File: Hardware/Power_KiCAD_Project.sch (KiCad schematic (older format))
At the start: 7 parts, among them J1 Barrel_Jack_MountingPin, J2 XT60 Cell 5, J3 XT60 Cell 4, J4 XT60 Cell 3, J5 XT60 Cell 2, J6 XT60 Cell 1, J7 XT60 To External Switch

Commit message: Routed GNDREF side of board
Correcting keepout silkscreen added 3mm to top and bottom, much appreciated!
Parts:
- J1: symbol Connector:Barrel_Jack_MountingPin -> RDT_Custom_Symbols:Barrel_Jack_MountingPin
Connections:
- net GND: now also J1.2, J1.3 (MountPin)
- removed net GNDREF: J1.2, J1.MP (MountPin)
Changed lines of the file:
@@
 Text Notes 9600 750  2    100  ~ 0
 Temperature Sensors
-$Sheet
-S 8250 2000 800  800
-U 61B35621
-F0 "MCP9808_2" 50
-F1 "COMPONENT_SHEETS/TEMPSENSOR_MCP9808.sch" 50
-F2 "SDA" I L 8250 2550 50
-F3 "SCL" I L 8250 2700 50
-F4 "A0" I R 9050 2150 50
-F5 "A1" I R 9050 2300 50
-F6 "A2" I R 9050 2450 50
-F7 "ALERT" I L 8250 2150 50
-$EndSheet
 Entry Wire Line
 	6750 1900 6650 1800
@@
 	3100 3500 3100 3150
 $Comp
-L power:GNDREF #PWR02
-U 1 1 61C61481
-P 1200 7300
-F 0 "#PWR02" H 1200 7050 50  0001 C CNN
-F 1 "GNDREF" H 1205 7127 50  0000 C CNN
-F 2 "" H 1200 7300 50  0001 C CNN
-F 3 "" H 1200 7300 50  0001 C CNN
-	1    1200 7300
-	1    0    0    -1
-$EndComp
-$Comp
 L Power_KiCAD_Project-rescue:XT60-M-XT60-M-Power_KiCAD_Project-rescue J6
 U 1 1 61C66D12
@@
 $EndComp
 $Comp
-L Connector:Barrel_Jack_MountingPin J1
+L RDT_Custom_Symbols:Barrel_Jack_MountingPin J1
 U 1 1 61C18157
 P 1300 2600
@@
 Wire Wire Line
 	1200 7300 1200 7050
-$Comp
-L power:GNDREF #PWR01
-U 1 1 61DF71F4
-P 950 2650
-F 0 "#PWR01" H 950 2400 50  0001 C CNN
-F 1 "GNDREF" H 955 2477 50  0000 C CNN
-F 2 "" H 950 2650 50  0001 C CNN
-F 3 "" H 950 2650 50  0001 C CNN
-	1    950  2650
-	1    0    0    -1
-$EndComp
 Entry Wire Line
 	3000 5900 3100 5800
@@
 NoConn ~ 5050 1700
 NoConn ~ 5050 1800
+$Comp
+L power:GND #PWR0101
+U 1 1 61FD97B5
+P 1200 7300
+AR Path="/61FD97B5" Ref="#PWR0101"  Part="1"
+AR Path="/61A48488/61FD97B5" Ref="#PWR?"  Part="1"
+F 0 "#PWR0101" H 1200 7050 50  0001 C CNN
+F 1 "GND" H 1205 7127 50  0000 C CNN
+F 2 "" H 1200 7300 50  0001 C CNN
+F 3 "" H 1200 7300 50  0001 C CNN
+	1    1200 7300
+	1    0    0    -1
+$EndComp
+$Sheet
+S 8250 2000 800  800
+U 61B35621
+F0 "MCP9808_2" 50
+F1 "COMPONENT_SHEETS/TEMPSENSOR_MCP9808.sch" 50
+F2 "SDA" I L 8250 2550 50
+F3 "SCL" I L 8250 2700 50
+F4 "A0" I R 9050 2150 50
+F5 "A1" I R 9050 2300 50
+F6 "A2" I R 9050 2450 50
+F7 "ALERT" I L 8250 2150 50
+$EndSheet
+$Comp
+L power:GND #PWR0102
+U 1 1 6208BBED
+P 950 2650
+AR Path="/6208BBED" Ref="#PWR0102"  Part="1"
+AR Path="/61A48488/6208BBED" Ref="#PWR?"  Part="1"
+F 0 "#PWR0102" H 950 2400 50  0001 C CNN
+F 1 "GND" H 955 2477 50  0000 C CNN
+F 2 "" H 950 2650 50  0001 C CNN
+F 3 "" H 950 2650 50  0001 C CNN
+	1    950  2650
+	1    0    0    -1
+$EndComp
 Wire Bus Line
 	7500 1600 7500 1800

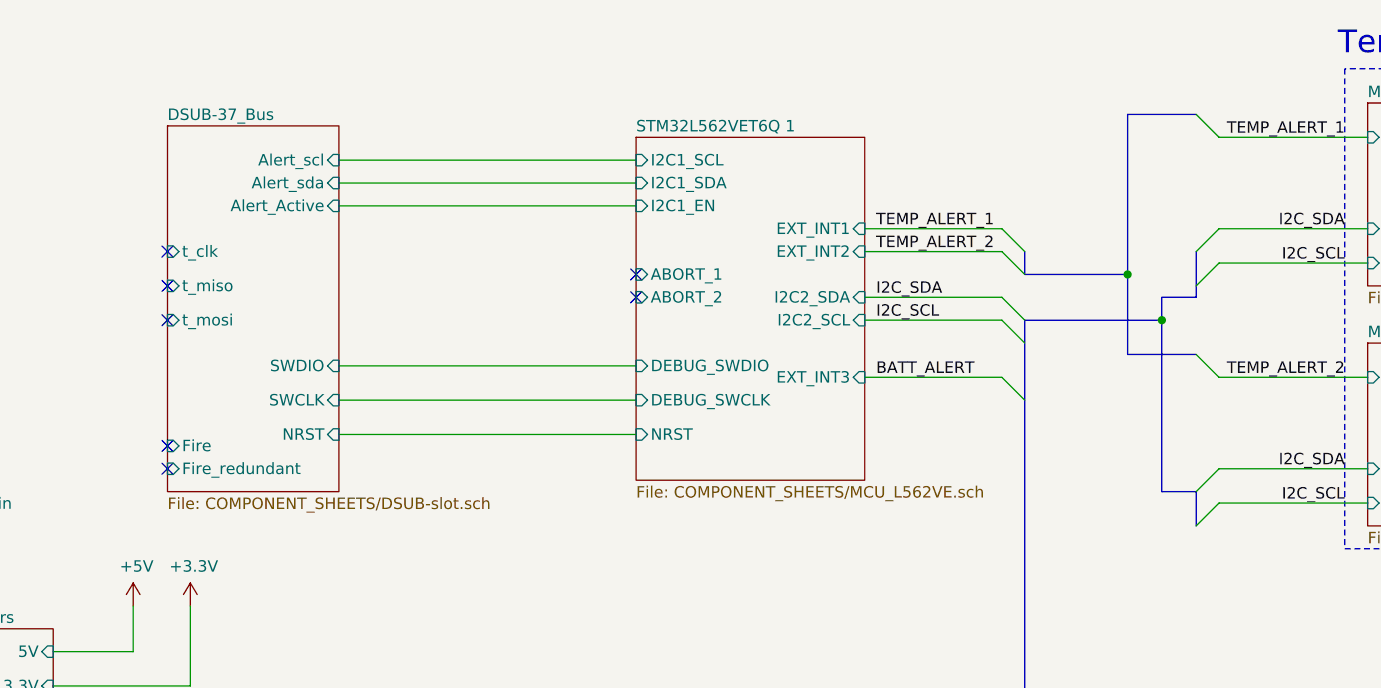
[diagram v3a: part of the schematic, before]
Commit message: Routed all connections and placed all components
MCU crystal still needs a ground peninsula
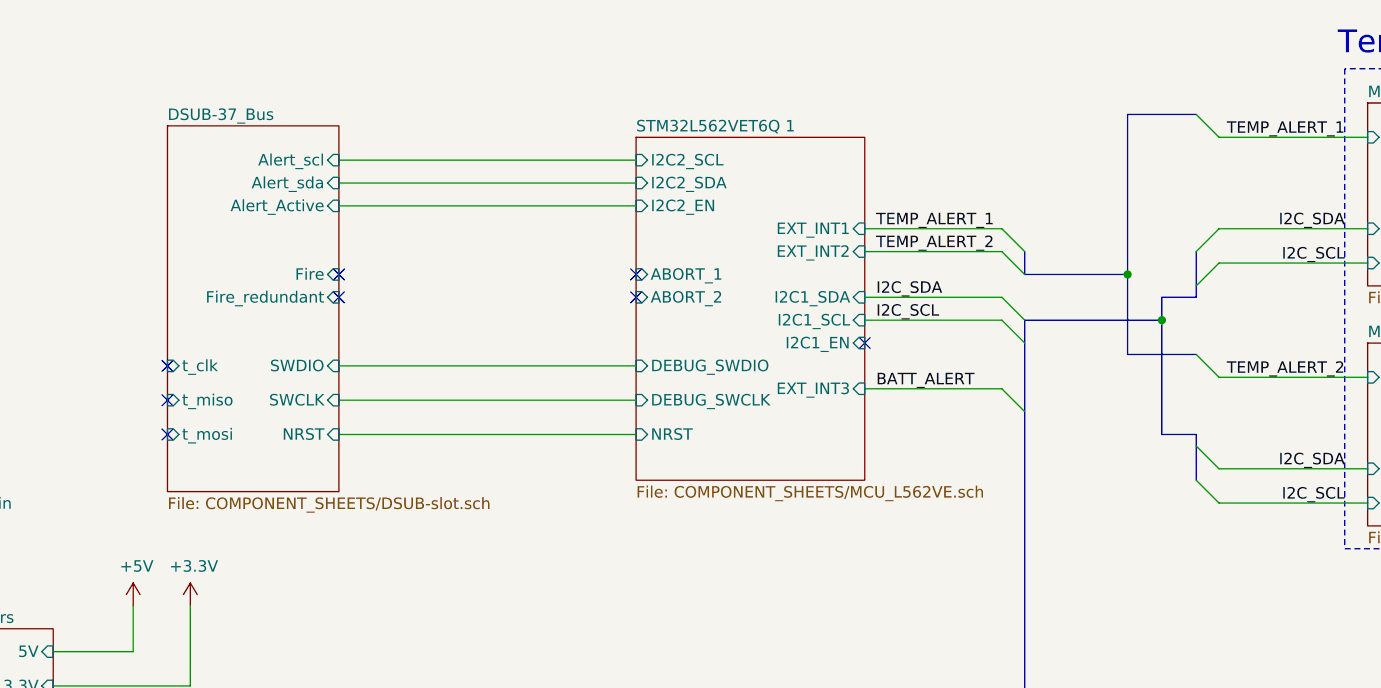
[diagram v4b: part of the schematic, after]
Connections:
- no-connect marks 7 -> 8
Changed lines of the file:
@@
 F0 "STM32L562VET6Q 1" 50
 F1 "COMPONENT_SHEETS/MCU_L562VE.sch" 50
-F2 "I2C1_SCL" I L 5050 1200 50
-F3 "I2C1_SDA" I L 5050 1300 50
+F2 "I2C1_SCL" I R 6050 1900 50
+F3 "I2C1_SDA" I R 6050 1800 50
 F4 "DEBUG_SWCLK" I L 5050 2250 50
 F5 "DEBUG_SWDIO" I L 5050 2100 50
@@
 F7 "ABORT_2" I L 5050 1800 50
 F8 "NRST" I L 5050 2400 50
-F9 "I2C2_SDA" I R 6050 1800 50
-F10 "I2C2_SCL" I R 6050 1900 50
-F11 "I2C1_EN" I L 5050 1400 50
+F9 "I2C2_SDA" I L 5050 1300 50
+F10 "I2C2_SCL" I L 5050 1200 50
+F11 "I2C1_EN" I R 6050 2000 50
 F12 "EXT_INT1" I R 6050 1500 50
 F13 "EXT_INT2" I R 6050 1600 50
-F14 "EXT_INT3" I R 6050 2150 50
+F14 "EXT_INT3" I R 6050 2200 50
+F15 "I2C2_EN" I L 5050 1400 50
 $EndSheet
-Text Label 6100 2150 0    50   ~ 0
+Text Label 6100 2200 0    50   ~ 0
 BATT_ALERT
 Text Notes 4650 5100 0    100  ~ 0
@@
 F0 "DSUB-37_Bus" 50
 F1 "COMPONENT_SHEETS/DSUB-slot.sch" 50
-F2 "t_mosi" I L 3000 1900 50
-F3 "t_miso" I L 3000 1750 50
-F4 "t_clk" I L 3000 1600 50
+F2 "t_mosi" I L 3000 2400 50
+F3 "t_miso" I L 3000 2250 50
+F4 "t_clk" I L 3000 2100 50
 F5 "Alert_scl" I R 3750 1200 50
 F6 "Alert_sda" I R 3750 1300 50
@@
 F9 "SWCLK" I R 3750 2250 50
 F10 "NRST" I R 3750 2400 50
-F11 "Fire" I L 3000 2450 50
-F12 "Fire_redundant" I L 3000 2550 50
+F11 "Fire" I R 3750 1700 50
+F12 "Fire_redundant" I R 3750 1800 50
 $EndSheet
 Wire Wire Line
@@
 	7600 1650 7500 1750
 Entry Wire Line
-	7600 2550 7500 2650
-Entry Wire Line
-	7600 2700 7500 2800
+	7500 2450 7600 2550
+Entry Wire Line
+	7500 2600 7600 2700
 Entry Wire Line
 	7600 2150 7500 2050
 Entry Wire Line
 	7600 1100 7500 1000
-Wire Bus Line
-	7500 2800 7500 2650
-Wire Bus Line
-	7500 2650 7350 2650
 Wire Bus Line
 	7200 1700 7200 1000
@@
 Connection ~ 7200 1700
 Wire Bus Line
-	7350 1900 7350 2650
+	7350 1900 7350 2400
 Wire Bus Line
 	7350 1900 7350 1800
@@
 BATT_ALERT
 Entry Wire Line
-	6750 2250 6650 2150
-Wire Wire Line
-	6650 2150 6050 2150
-NoConn ~ 3000 1600
-NoConn ~ 3000 1750
-NoConn ~ 3000 1900
-NoConn ~ 3000 2450
-NoConn ~ 3000 2550
+	6750 2300 6650 2200
+NoConn ~ 3000 2100
+NoConn ~ 3000 2250
+NoConn ~ 3000 2400
 Wire Wire Line
 	1200 2900 1200 7050
@@
 Wire Wire Line
 	1400 3600 1400 2900
-NoConn ~ 5050 1700
-NoConn ~ 5050 1800
 $Comp
 L power:GND #PWR0101
@@
 	1    0    0    -1
 $EndComp
+NoConn ~ 5050 1700
+NoConn ~ 5050 1800
+NoConn ~ 3750 1700
+NoConn ~ 3750 1800
+Wire Wire Line
+	6650 2200 6050 2200
+NoConn ~ 6050 2000
+Wire Bus Line
+	7350 2400 7500 2400
 Wire Bus Line
 	7500 1600 7500 1800
 Wire Bus Line
+	7500 2400 7500 2600
+Wire Bus Line
 	3100 5250 3100 5800
